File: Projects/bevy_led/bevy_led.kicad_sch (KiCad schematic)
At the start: 78 parts, among them J1 USB_C_Receptacle_USB2.0, SW1 SW_Push, SW2 SW_Push, SW3 SW_Push, SW4 SW_Push, U1 DRTR5V0U4S, U2 ESP32-S3-MINI-1, U3 74AHCT1G125, U4 XC6222B331MR-G

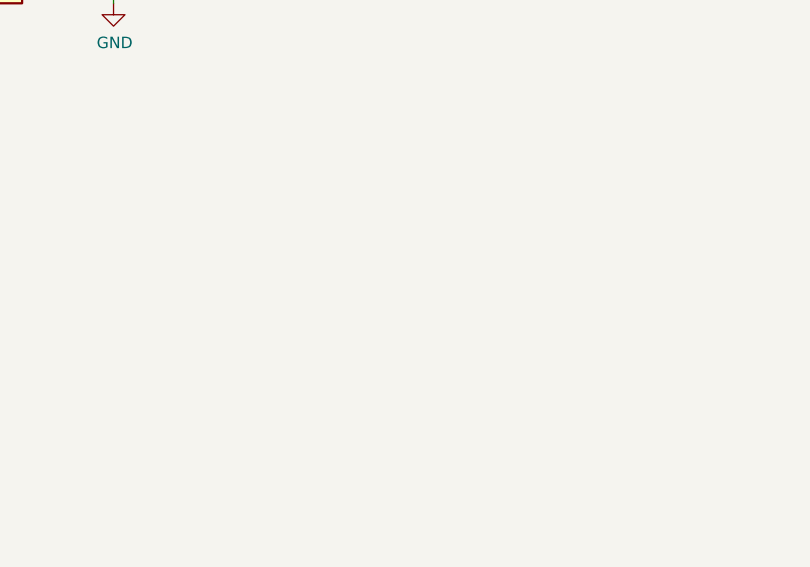
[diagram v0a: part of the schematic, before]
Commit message: Update board outline and add SAO header
TODO: figure out how to power from SAO or add battery.

Signed-off-by: Michael Welling <mwelling79@gmail.com>
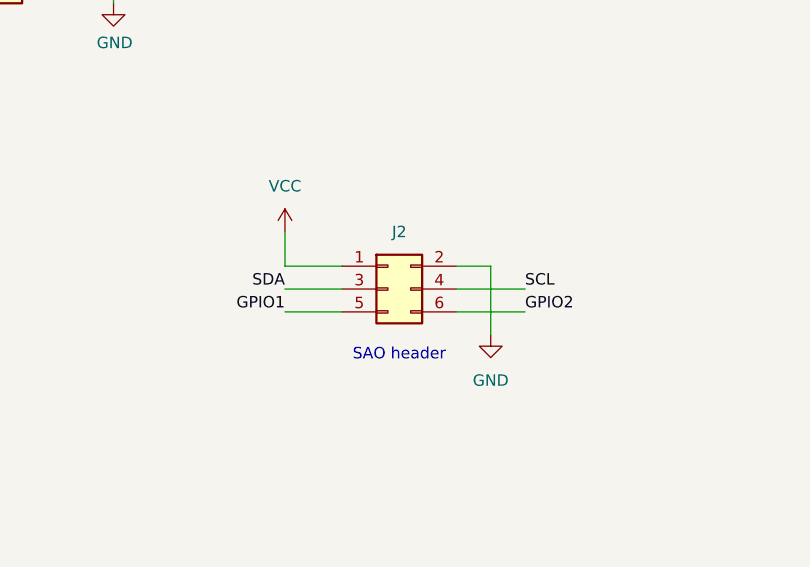
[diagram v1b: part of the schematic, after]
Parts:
- added J2: Conn_02x03_Odd_Even, Connector_PinHeader_2.54mm:PinHeader_2x03_P2.54mm_Vertical, symbol Connector_Generic:Conn_02x03_Odd_Even
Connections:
- net GND: now also J2.2 (Pin_2)
- new net GPIO1: J2.5 (Pin_5)
- new net GPIO2: J2.6 (Pin_6)
- new net SCL: J2.4 (Pin_4)
- new net SDA: J2.3 (Pin_3)
- new net VCC: J2.1 (Pin_1)
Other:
- note added: "SAO header"

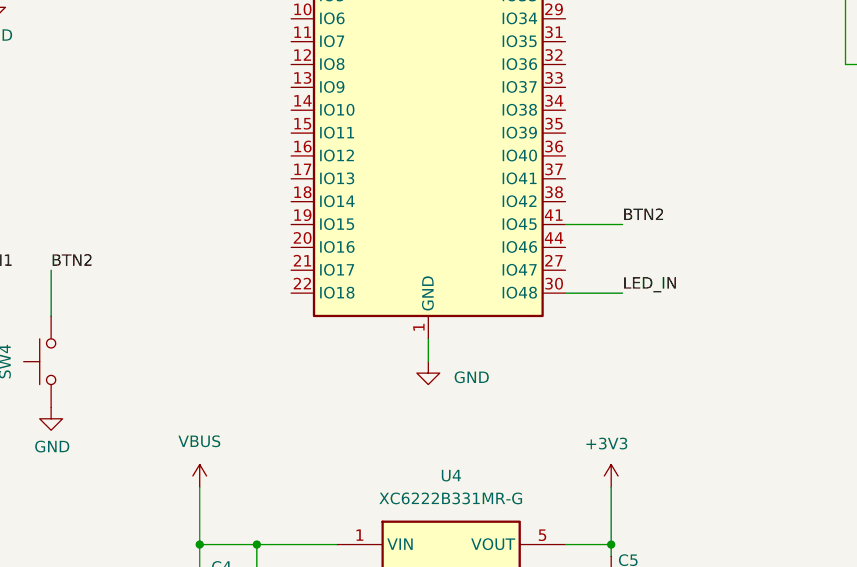
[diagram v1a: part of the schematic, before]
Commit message: Update to sane LED ordering
Signed-off-by: Michael Welling <mwelling79@gmail.com>
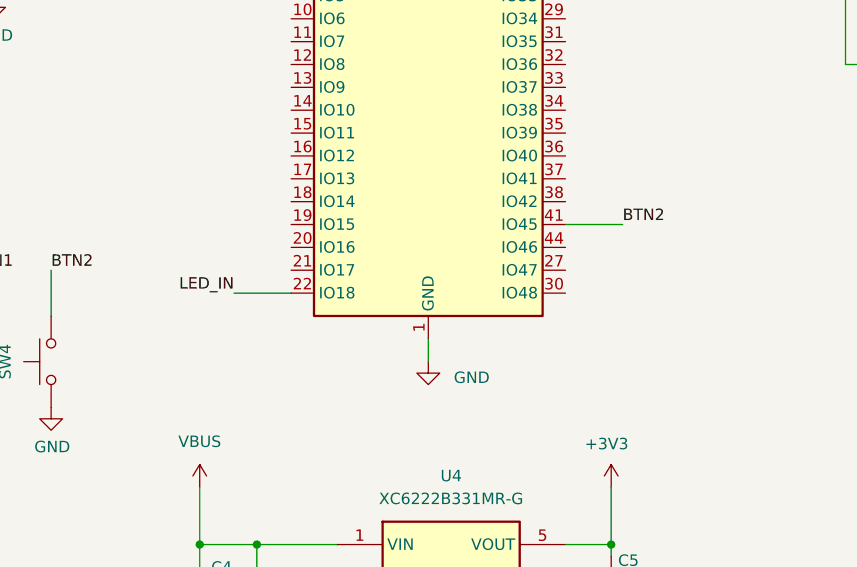
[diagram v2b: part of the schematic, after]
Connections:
- net LED_IN: now also U2.22 (IO18); no longer U2.30 (IO48)
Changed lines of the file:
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@@
 	(wire
 		(pts
-			(xy 113.03 93.98) (xy 119.38 93.98)
+			(xy 82.55 93.98) (xy 76.2 93.98)
 		)
 		(stroke
@@
 	)
 	(label "LED_IN"
-		(at 119.38 93.98 0)
+		(at 76.2 93.98 180)
 		(effects
 			(font
 				(size 1.27 1.27)
 			)
-			(justify left bottom)
-		)
-	)
+			(justify right bottom)
+		)
+	)
